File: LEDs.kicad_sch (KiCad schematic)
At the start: 62 parts, among them J5 Case Lighting

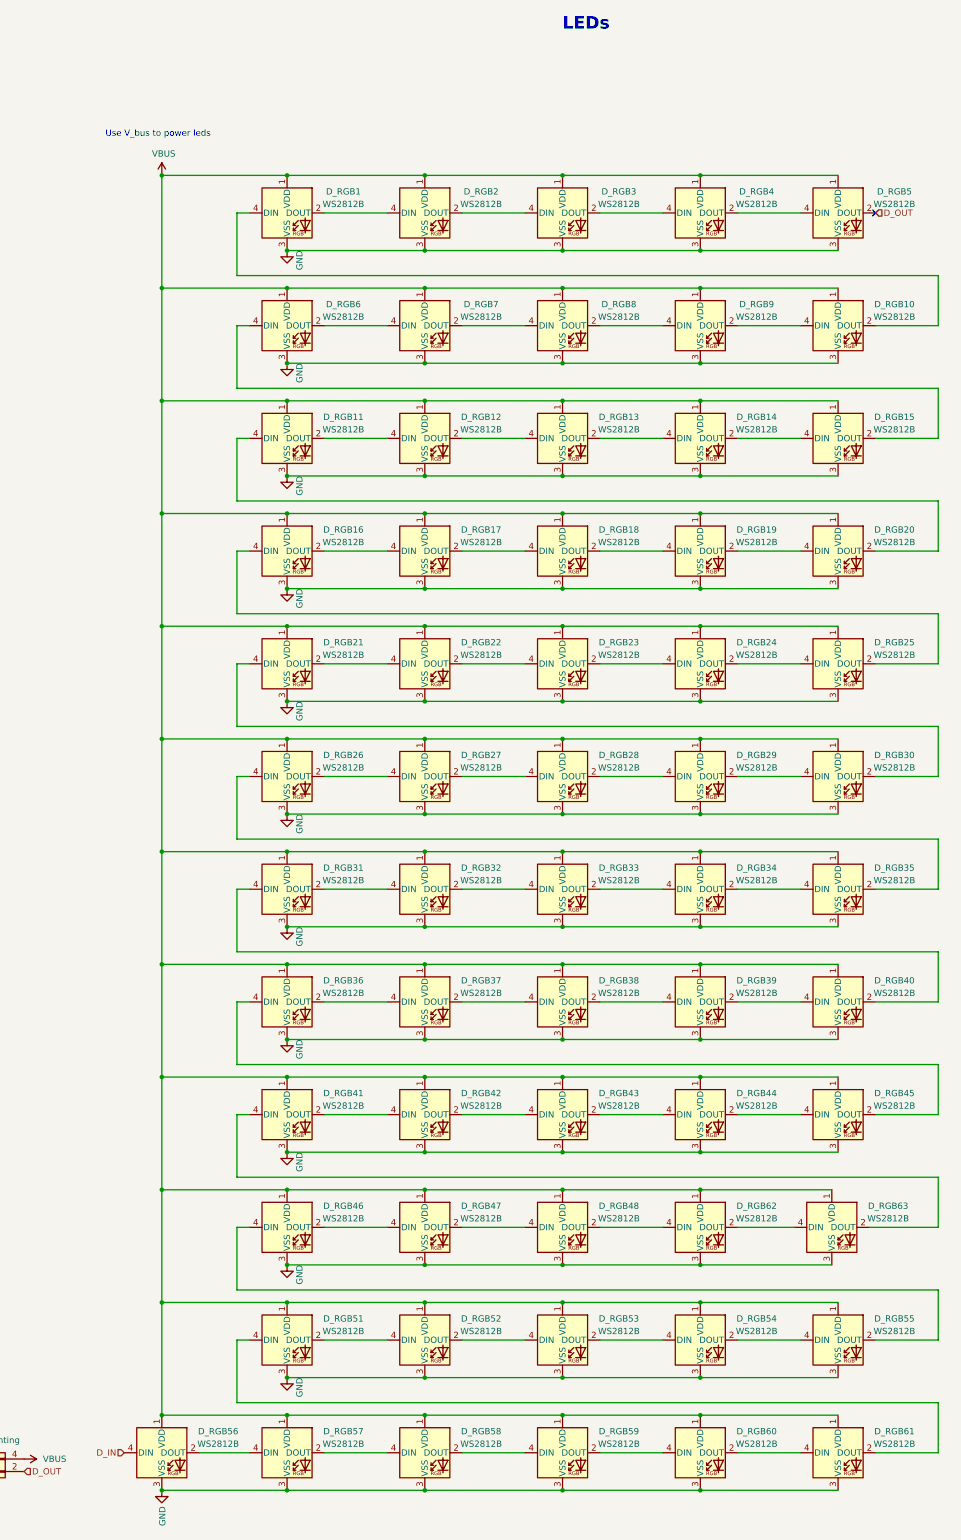
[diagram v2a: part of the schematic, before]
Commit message: routing, rotate leds to make tracks easier
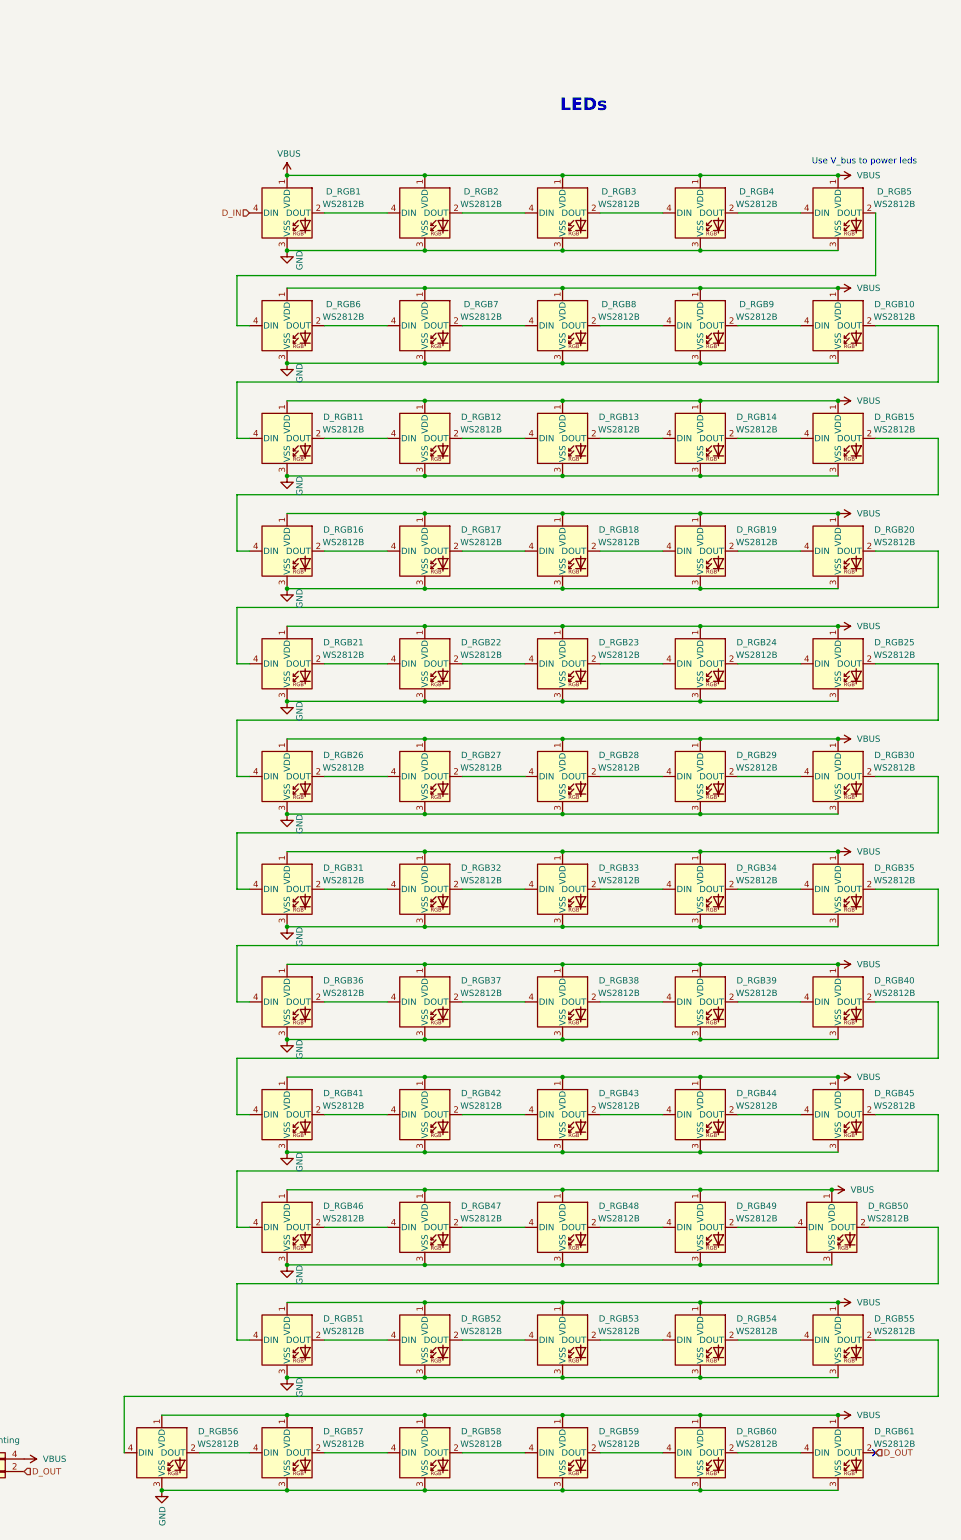
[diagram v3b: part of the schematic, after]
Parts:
- renumbered D_RGB62 to D_RGB49, D_RGB63 to D_RGB50
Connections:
- net D_IN: now also D_RGB1.4 (DIN); no longer D_RGB56.4 (DIN)
- net D_OUT: now also D_RGB61.2 (DOUT); no longer D_RGB5.2 (DOUT)
- net at D_RGB11.4 (DIN): now also D_RGB10.2 (DOUT); no longer D_RGB20.2 (DOUT)
- net at D_RGB16.4 (DIN): now also D_RGB15.2 (DOUT); no longer D_RGB25.2 (DOUT)
- net at D_RGB26.4 (DIN): now also D_RGB25.2 (DOUT); no longer D_RGB35.2 (DOUT)
- net at D_RGB31.4 (DIN): now also D_RGB30.2 (DOUT); no longer D_RGB40.2 (DOUT)
- net at D_RGB21.4 (DIN): now also D_RGB20.2 (DOUT); no longer D_RGB30.2 (DOUT)
- net at D_RGB6.4 (DIN): now also D_RGB5.2 (DOUT); no longer D_RGB15.2 (DOUT)
- net at D_RGB41.4 (DIN): now also D_RGB40.2 (DOUT); no longer D_RGB50.2 (DOUT)
- net at D_RGB36.4 (DIN): now also D_RGB35.2 (DOUT); no longer D_RGB45.2 (DOUT)
- net at D_RGB55.2 (DOUT): now also D_RGB56.4 (DIN); no longer D_RGB46.4 (DIN)
- net at D_RGB51.4 (DIN): now also D_RGB50.2 (DOUT); no longer D_RGB61.2 (DOUT)
- new net: D_RGB45.2 (DOUT), D_RGB46.4 (DIN)

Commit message: pretty much done
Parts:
- added JP1, JP6, JP7, JP8: Jumper_2_Bridged, Jumper:SolderJumper-2_P1.3mm_Open_RoundedPad1.0x1.5mm, symbol Jumper:Jumper_2_Bridged
- J5: footprint Connector_JST:JST_PH_S4B-PH-K_1x04_P2.00mm_Horizontal -> Connector_PinHeader_2.54mm:PinHeader_1x04_P2.54mm_Vertical; now not fitted; now left out of the parts list
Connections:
- net at D_RGB14.2 (DOUT): now also JP1.1 (A); no longer D_RGB15.4 (DIN)
- net at D_RGB46.2 (DOUT): now also JP7.1 (A); no longer D_RGB47.4 (DIN)
- net at D_RGB50.2 (DOUT): now also JP8.1 (A); no longer D_RGB51.4 (DIN)
- net at D_RGB18.2 (DOUT): now also JP6.1 (A); no longer D_RGB19.4 (DIN)
- new net: D_RGB51.4 (DIN), JP8.2 (B)
- new net: D_RGB19.4 (DIN), JP6.2 (B)
- new net: D_RGB47.4 (DIN), JP7.2 (B)
- new net: D_RGB15.4 (DIN), JP1.2 (B)

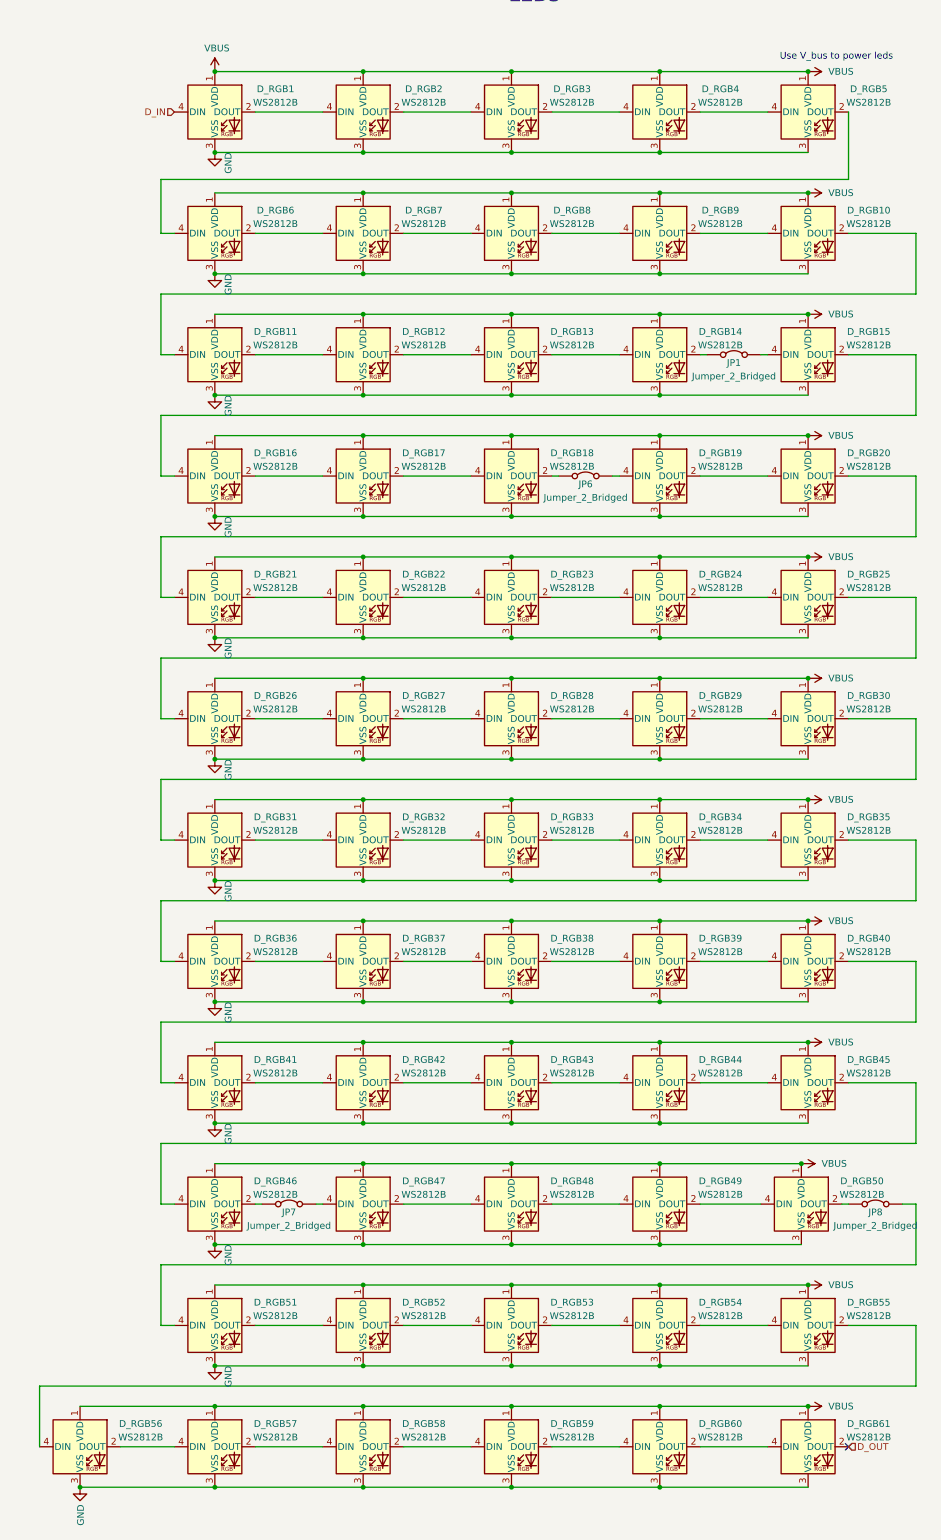
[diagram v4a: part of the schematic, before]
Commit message: test prod files for jlc quote, wrong diode footprint 🤦‍
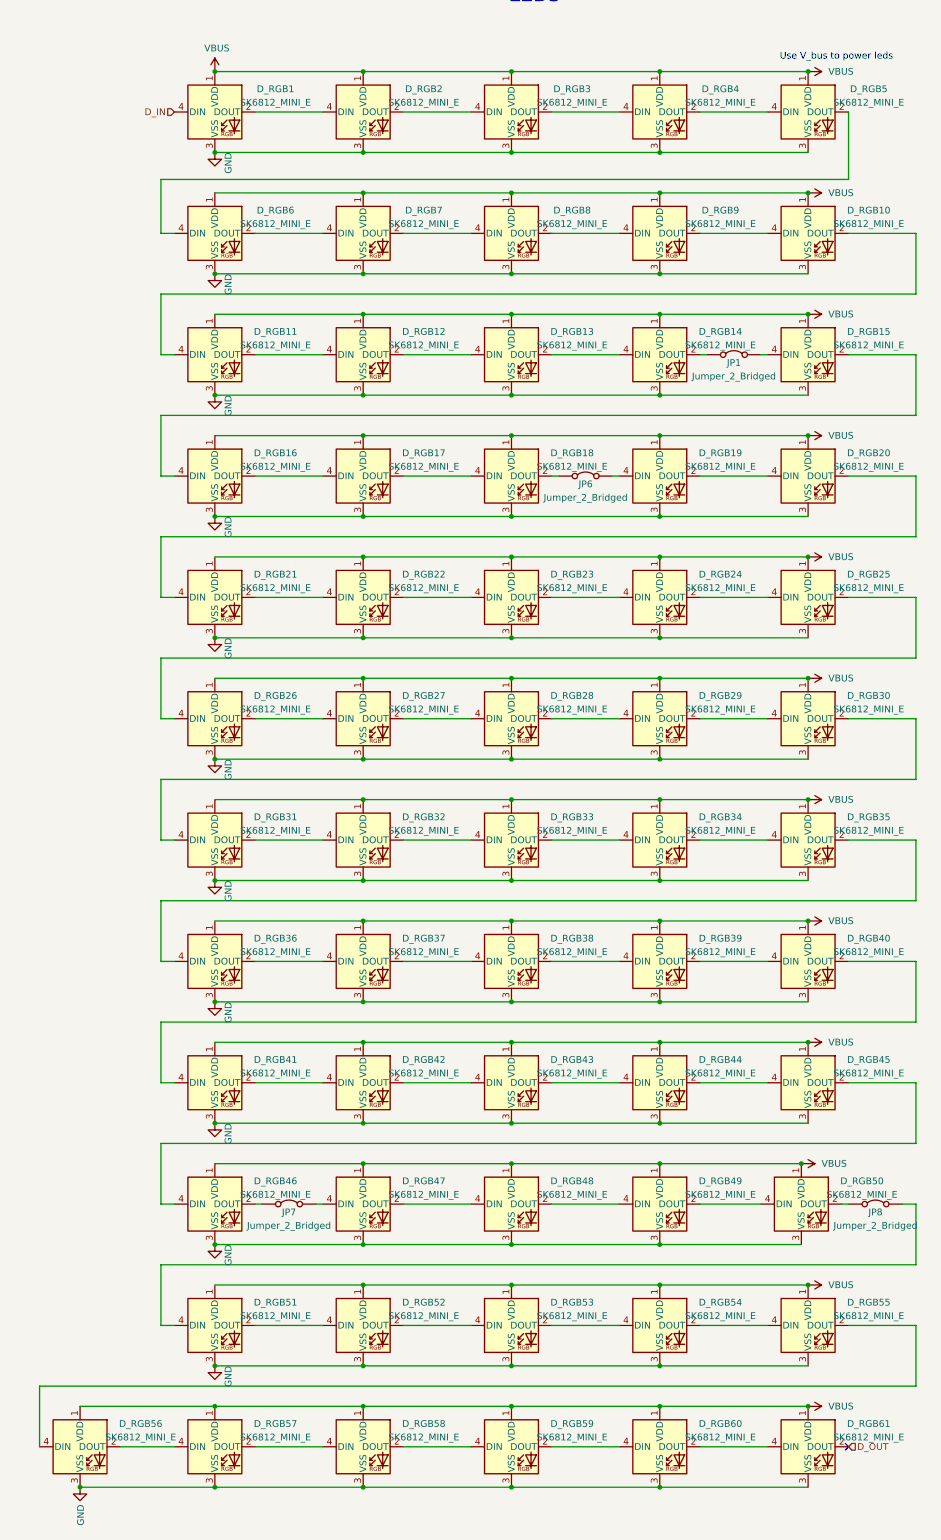
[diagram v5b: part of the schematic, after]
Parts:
- D_RGB1, D_RGB10, D_RGB11, D_RGB12, D_RGB13, D_RGB14, D_RGB15, D_RGB16, D_RGB17, D_RGB18, D_RGB19, D_RGB2, D_RGB20, D_RGB21, D_RGB22, D_RGB23, D_RGB24, D_RGB25, D_RGB26, D_RGB27, D_RGB28, D_RGB29, D_RGB3, D_RGB30, D_RGB31, D_RGB32, D_RGB33, D_RGB34, D_RGB35, D_RGB36, D_RGB37, D_RGB38, D_RGB39, D_RGB4, D_RGB40, D_RGB41, D_RGB42, D_RGB43, D_RGB44, D_RGB45, D_RGB46, D_RGB47, D_RGB48, D_RGB49, D_RGB5, D_RGB50, D_RGB51, D_RGB52, D_RGB53, D_RGB54, D_RGB55, D_RGB56, D_RGB57, D_RGB58, D_RGB59, D_RGB6, D_RGB60, D_RGB61, D_RGB7, D_RGB8, D_RGB9: value WS2812B -> SK6812_MINI_E
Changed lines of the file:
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@@
 			)
 		)
-		(property "Value" "WS2812B"
+		(property "Value" "SK6812_MINI_E"
 			(at 102.87 126.4793 0)
 			(effects
@@
 			)
 		)
-		(property "Value" "WS2812B"
+		(property "Value" "SK6812_MINI_E"
 			(at 158.75 332.2193 0)
 			(effects
@@
 			)
 		)
-		(property "Value" "WS2812B"
+		(property "Value" "SK6812_MINI_E"
 			(at 130.81 332.2193 0)
 			(effects
@@
 			)
 		)
-		(property "Value" "WS2812B"
+		(property "Value" "SK6812_MINI_E"
 			(at 130.81 309.3593 0)
 			(effects
@@
 			)
 		)
-		(property "Value" "WS2812B"
+		(property "Value" "SK6812_MINI_E"
 			(at 102.87 332.2193 0)
 			(effects
@@
 			)
 		)
-		(property "Value" "WS2812B"
+		(property "Value" "SK6812_MINI_E"
 			(at 102.87 149.3393 0)
 			(effects
@@
 			)
 		)
-		(property "Value" "WS2812B"
+		(property "Value" "SK6812_MINI_E"
 			(at 186.69 286.4993 0)
 			(effects
@@
 			)
 		)
-		(property "Value" "WS2812B"
+		(property "Value" "SK6812_MINI_E"
 			(at 186.69 332.2193 0)
 			(effects
@@
 			)
 		)
-		(property "Value" "WS2812B"
+		(property "Value" "SK6812_MINI_E"
 			(at 130.81 263.6393 0)
 			(effects
@@
 			)
 		)
-		(property "Value" "WS2812B"
+		(property "Value" "SK6812_MINI_E"
 			(at 186.69 240.7793 0)
 			(effects
@@
 			)
 		)
-		(property "Value" "WS2812B"
+		(property "Value" "SK6812_MINI_E"
 			(at 102.87 195.0593 0)
 			(effects
@@
 			)
 		)
-		(property "Value" "WS2812B"
+		(property "Value" "SK6812_MINI_E"
 			(at 130.81 126.4793 0)
 			(effects
@@
 			)
 		)
-		(property "Value" "WS2812B"
+		(property "Value" "SK6812_MINI_E"
 			(at 102.87 217.9193 0)
 			(effects
@@
 			)
 		)
-		(property "Value" "WS2812B"
+		(property "Value" "SK6812_MINI_E"
 			(at 130.81 80.7593 0)
 			(effects
@@
 			)
 		)
-		(property "Value" "WS2812B"
+		(property "Value" "SK6812_MINI_E"
 			(at 77.47 332.2193 0)
 			(effects
@@
 			)
 		)
-		(property "Value" "WS2812B"
+		(property "Value" "SK6812_MINI_E"
 			(at 186.69 195.0593 0)
 			(effects
@@
 			)
 		)
-		(property "Value" "WS2812B"
+		(property "Value" "SK6812_MINI_E"
 			(at 186.69 126.4793 0)
 			(effects
@@
 			)
 		)
-		(property "Value" "WS2812B"
+		(property "Value" "SK6812_MINI_E"
 			(at 158.75 103.6193 0)
 			(effects
@@
 			)
 		)
-		(property "Value" "WS2812B"
+		(property "Value" "SK6812_MINI_E"
 			(at 186.69 103.6193 0)
 			(effects
@@
 			)
 		)
-		(property "Value" "WS2812B"
+		(property "Value" "SK6812_MINI_E"
 			(at 158.75 263.6393 0)
 			(effects
@@
 			)
 		)
-		(property "Value" "WS2812B"
+		(property "Value" "SK6812_MINI_E"
 			(at 214.63 217.9193 0)
 			(effects
@@
 			)
 		)
-		(property "Value" "WS2812B"
+		(property "Value" "SK6812_MINI_E"
 			(at 186.69 263.6393 0)
 			(effects
@@
 			)
 		)
-		(property "Value" "WS2812B"
+		(property "Value" "SK6812_MINI_E"
 			(at 102.87 172.1993 0)
 			(effects
@@
 			)
 		)
-		(property "Value" "WS2812B"
+		(property "Value" "SK6812_MINI_E"
 			(at 102.87 103.6193 0)
 			(effects
@@
 			)
 		)
-		(property "Value" "WS2812B"
+		(property "Value" "SK6812_MINI_E"
 			(at 102.87 263.6393 0)
 			(effects
@@
 			)
 		)
-		(property "Value" "WS2812B"
+		(property "Value" "SK6812_MINI_E"
 			(at 102.87 240.7793 0)
 			(effects
@@
 			)
 		)
-		(property "Value" "WS2812B"
+		(property "Value" "SK6812_MINI_E"
 			(at 158.75 240.7793 0)
 			(effects
@@
 			)
 		)
-		(property "Value" "WS2812B"
+		(property "Value" "SK6812_MINI_E"
 			(at 102.87 286.4993 0)
 			(effects
@@
 			)
 		)
-		(property "Value" "WS2812B"
+		(property "Value" "SK6812_MINI_E"
 			(at 130.81 172.1993 0)
 			(effects
@@
 			)
 		)
-		(property "Value" "WS2812B"
+		(property "Value" "SK6812_MINI_E"
 			(at 186.69 172.1993 0)
 			(effects
@@
 			)
 		)
-		(property "Value" "WS2812B"
+		(property "Value" "SK6812_MINI_E"
 			(at 158.75 309.3593 0)
 			(effects
@@
 			)
 		)
-		(property "Value" "WS2812B"
+		(property "Value" "SK6812_MINI_E"
 			(at 214.63 195.0593 0)
 			(effects
@@
 			)
 		)
-		(property "Value" "WS2812B"
+		(property "Value" "SK6812_MINI_E"
 			(at 186.69 217.9193 0)
 			(effects
@@
 			)
 		)
-		(property "Value" "WS2812B"
+		(property "Value" "SK6812_MINI_E"
 			(at 158.75 286.4993 0)
 			(effects
@@
 			)
 		)
-		(property "Value" "WS2812B"
+		(property "Value" "SK6812_MINI_E"
 			(at 158.75 126.4793 0)
 			(effects
@@
 			)
 		)
-		(property "Value" "WS2812B"
+		(property "Value" "SK6812_MINI_E"
 			(at 214.63 103.6193 0)
 			(effects
@@
 			)
 		)
-		(property "Value" "WS2812B"
+		(property "Value" "SK6812_MINI_E"
 			(at 102.87 309.3593 0)
 			(effects
@@
 			)
 		)
-		(property "Value" "WS2812B"
+		(property "Value" "SK6812_MINI_E"
 			(at 186.69 309.3593 0)
 			(effects
@@
 			)
 		)
-		(property "Value" "WS2812B"
+		(property "Value" "SK6812_MINI_E"
 			(at 214.63 263.6393 0)
 			(effects
@@
 			)
 		)
-		(property "Value" "WS2812B"
+		(property "Value" "SK6812_MINI_E"
 			(at 158.75 217.9193 0)
 			(effects
@@
 			)
 		)
-		(property "Value" "WS2812B"
+		(property "Value" "SK6812_MINI_E"
 			(at 214.63 332.2193 0)
 			(effects
@@
 			)
 		)
-		(property "Value" "WS2812B"
+		(property "Value" "SK6812_MINI_E"
 			(at 186.69 80.7593 0)
 			(effects
@@
 			)
 		)
-		(property "Value" "WS2812B"
+		(property "Value" "SK6812_MINI_E"
 			(at 158.75 195.0593 0)
 			(effects
@@
 			)
 		)
-		(property "Value" "WS2812B"
+		(property "Value" "SK6812_MINI_E"
 			(at 214.63 309.3593 0)
 			(effects
@@
 			)
 		)
-		(property "Value" "WS2812B"
+		(property "Value" "SK6812_MINI_E"
 			(at 130.81 149.3393 0)
 			(effects
@@
 			)
 		)
-		(property "Value" "WS2812B"
+		(property "Value" "SK6812_MINI_E"
 			(at 158.75 149.3393 0)
 			(effects
@@
 			)
 		)
-		(property "Value" "WS2812B"
+		(property "Value" "SK6812_MINI_E"
 			(at 130.81 195.0593 0)
 			(effects
@@
 			)
 		)
-		(property "Value" "WS2812B"
+		(property "Value" "SK6812_MINI_E"
 			(at 130.81 103.6193 0)
 			(effects
@@
 			)
 		)
-		(property "Value" "WS2812B"
+		(property "Value" "SK6812_MINI_E"
 			(at 214.63 172.1993 0)
 			(effects
@@
 			)
 		)
-		(property "Value" "WS2812B"
+		(property "Value" "SK6812_MINI_E"
 			(at 158.75 80.7593 0)
 			(effects
@@
 			)
 		)
-		(property "Value" "WS2812B"
+		(property "Value" "SK6812_MINI_E"
 			(at 186.69 149.3393 0)
 			(effects
@@
 			)
 		)
-		(property "Value" "WS2812B"
+		(property "Value" "SK6812_MINI_E"
 			(at 214.63 149.3393 0)
 			(effects
@@
 			)
 		)
-		(property "Value" "WS2812B"
+		(property "Value" "SK6812_MINI_E"
 			(at 214.63 80.7593 0)
 			(effects
@@
 			)
 		)
-		(property "Value" "WS2812B"
+		(property "Value" "SK6812_MINI_E"
 			(at 130.81 286.4993 0)
 			(effects
@@
 			)
 		)
-		(property "Value" "WS2812B"
+		(property "Value" "SK6812_MINI_E"
 			(at 102.87 80.7593 0)
 			(effects
@@
 			)
 		)
-		(property "Value" "WS2812B"
+		(property "Value" "SK6812_MINI_E"
 			(at 214.63 240.7793 0)
 			(effects
@@
 			)
 		)
-		(property "Value" "WS2812B"
+		(property "Value" "SK6812_MINI_E"
 			(at 158.75 172.1993 0)
 			(effects
@@
 			)
 		)
-		(property "Value" "WS2812B"
+		(property "Value" "SK6812_MINI_E"
 			(at 214.63 126.4793 0)
 			(effects
@@
 			)
 		)
-		(property "Value" "WS2812B"
+		(property "Value" "SK6812_MINI_E"
 			(at 130.81 217.9193 0)
 			(effects
@@
 			)
 		)
-		(property "Value" "WS2812B"
+		(property "Value" "SK6812_MINI_E"
 			(at 213.36 286.4993 0)
 			(effects
@@
 			)
 		)
-		(property "Value" "WS2812B"
+		(property "Value" "SK6812_MINI_E"
 			(at 130.81 240.7793 0)
 			(effects

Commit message: add part nums for bom
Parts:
- D_RGB1, D_RGB10, D_RGB11, D_RGB12, D_RGB13, D_RGB14, D_RGB15, D_RGB16, D_RGB17, D_RGB18, D_RGB19, D_RGB2, D_RGB20, D_RGB21, D_RGB22, D_RGB23, D_RGB24, D_RGB25, D_RGB26, D_RGB27, D_RGB28, D_RGB29, D_RGB3, D_RGB30, D_RGB31, D_RGB32, D_RGB33, D_RGB34, D_RGB35, D_RGB36, D_RGB37, D_RGB38, D_RGB39, D_RGB4, D_RGB40, D_RGB41, D_RGB42, D_RGB43, D_RGB44, D_RGB45, D_RGB46, D_RGB47, D_RGB48, D_RGB49, D_RGB5, D_RGB50, D_RGB51, D_RGB52, D_RGB53, D_RGB54, D_RGB55, D_RGB56, D_RGB57, D_RGB58, D_RGB59, D_RGB6, D_RGB60, D_RGB61, D_RGB7, D_RGB8, D_RGB9: Comment (none) -> Do Not Substitute; LCSC (none) -> C5149201; MPN (none) -> SK6812MINI-E; Manufacturer (none) -> OPSCO Optoelectronics; Type (none) -> SMD
- J5: Type (none) -> DNS
- JP1, JP6, JP7, JP8: now left out of the parts list
